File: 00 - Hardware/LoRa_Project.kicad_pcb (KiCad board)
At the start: 4 copper layers, 60 x 45 mm, 82 parts, among them IC1 MAX17048G+T10, IC2 E22-900M22S, J1 Conn_01x04_Pin, J2 USB_C_Receptacle_USB2.0_16P, J3 Conn_01x04_Pin, J4 Header_01x02_2.0mm JST PH, J5 SMA_ST_SMD, J6 Conn_01x04_Pin, U1 TPS2116DRLR, U2 MIC5219-3.3YM5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

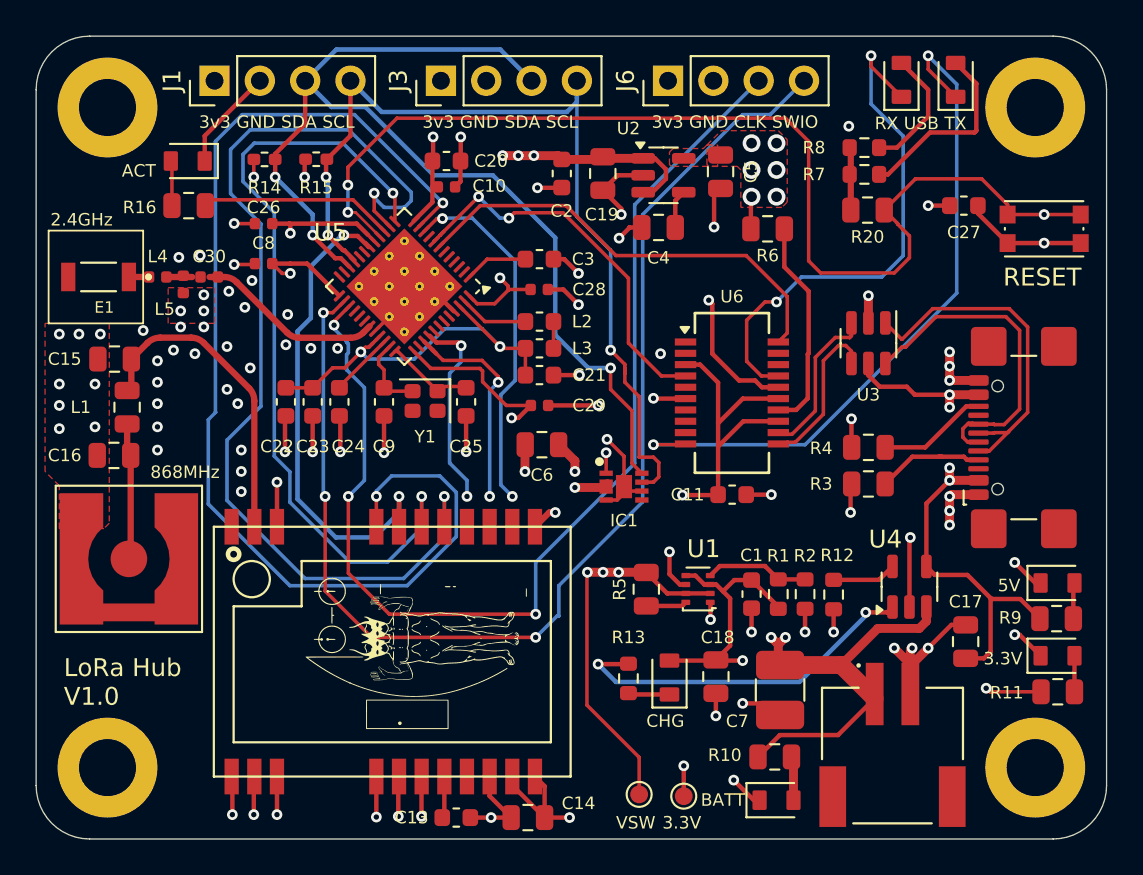
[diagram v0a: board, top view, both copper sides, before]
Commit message: updated FDTI cbus connections
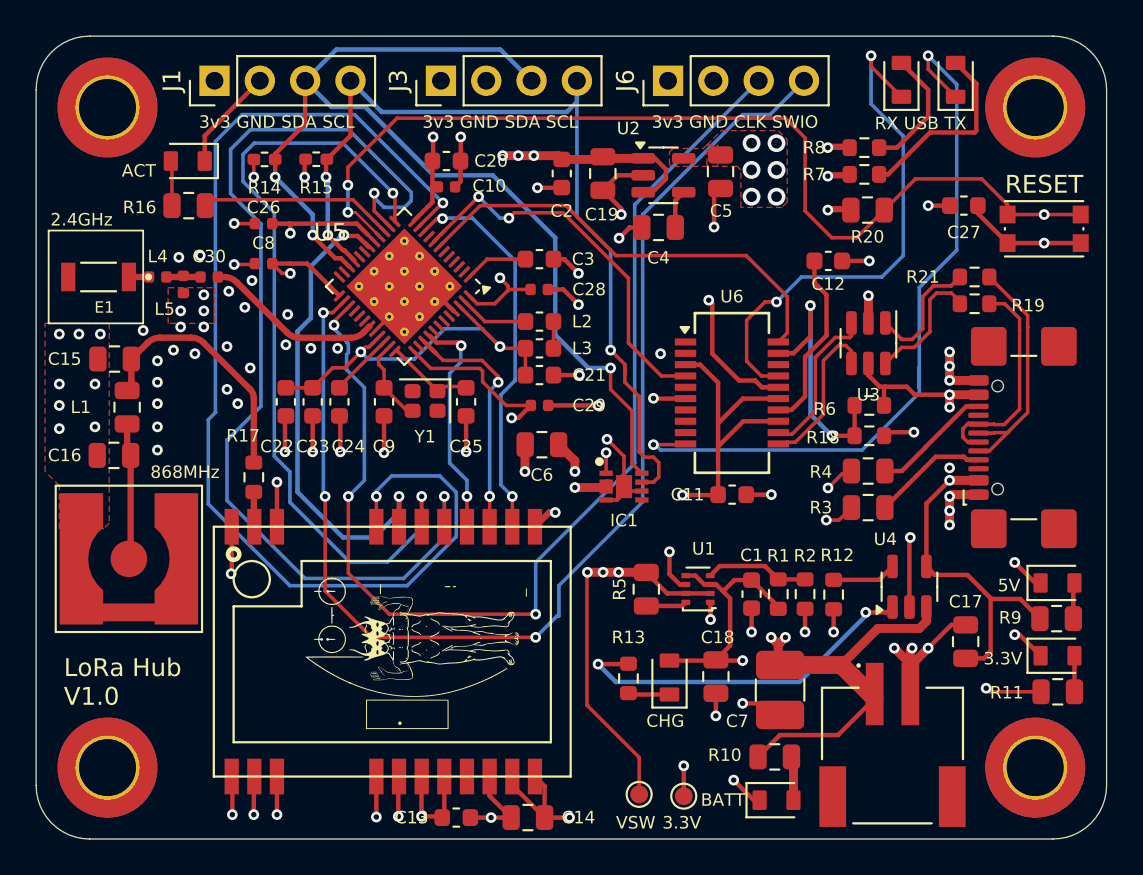
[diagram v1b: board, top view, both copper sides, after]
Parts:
- added C12: 100nF, Capacitor_SMD:C_0603_1608Metric, F.Cu at (234.4, 64.6)
- added R17: 0R_0603, Resistor_SMD:R_0603_1608Metric, F.Cu at (202.2, 76.7)
- added R18: 10K, Resistor_SMD:R_0603_1608Metric, F.Cu at (236.7, 74.4)
- added R19: 27, Resistor_SMD:R_0603_1608Metric, F.Cu at (242.6, 67.0)
- added R21: 27, Resistor_SMD:R_0603_1608Metric, F.Cu at (242.6, 65.5)
- H1, H2, H3, H4: value MountingHole_M3 -> MountingHole_Pad_M3; footprint Project_Footprints:MountingHole_3.2mm_M3_DIN965_Pad -> MountingHole:MountingHole_3.2mm_M3_DIN965_Pad_TopBottom
- R6: value 10K_0805 -> 4k7; footprint Project_Footprints:R_0805_2012Metric -> Resistor_SMD:R_0603_1608Metric
- moved R6 11.4 mm to (236.7, 72.7), turned to 180 degrees
- moved R3 1.33 mm to (236.6, 78.4)
- moved R4 1.33 mm to (236.6, 76.4)
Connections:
- C15 pad 1: Net-(IC2-ANT) -> Net-(C15-Pad1)
- L1 pad 1: Net-(IC2-ANT) -> Net-(C15-Pad1)
- R6 pad 1: +3V3 -> VBUS
- R6 pad 2: Net-(U6-~{RESET}) -> Net-(U6-CBUS3)
- U3 pad 1: /Power/USB_D- -> Net-(R21-Pad2)
- U3 pad 6: /Power/USB_D+ -> Net-(R19-Pad2)
- U5 pad 41: (no net) -> unconnected-(U5-P0.28-Pad41)
- U5 pad 42: (no net) -> unconnected-(U5-P0.29-Pad42)
- U5 pad 43: (no net) -> unconnected-(U5-P0.30-Pad43)
- U5 pad 44: (no net) -> unconnected-(U5-P0.31-Pad44)
- U5 pad 6: (no net) -> unconnected-(U5-P0.07-Pad6)
- U6 pad 19: unconnected-(U6-CBUS3-Pad19) -> Net-(U6-CBUS3)
- Y1 pad 2: Net-(U5-XC1) -> (no net)
- Y1 pad 3: (no net) -> Net-(U5-XC1)
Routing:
- net Net-(IC2-ANT): track 17.9 -> 1.96 mm
- net Net-(U6-CBUS3): track 0.00 -> 14.7 mm, vias 0 -> 2
- net Net-(C15-Pad1): track 0.00 -> 14.2 mm
- net Net-(R19-Pad2): track 0.00 -> 7.19 mm
- net Net-(R21-Pad2): track 0.00 -> 7.09 mm
- net Net-(U5-~{RESET}): track 61.5 -> 54.8 mm
- net GND: track 148.3 -> 154.7 mm
- net /Power/USB_D+: track 18.5 -> 12.3 mm
- net /Power/USB_D-: track 19.7 -> 13.9 mm
- net /Peripherals/TXLED: track 39.1 -> 42.6 mm
- net Net-(U6-~{RESET}): track 12.0 -> 10.2 mm
- net +3V3: track 68.3 -> 66.5 mm, vias 18 -> 20
- net /nRF52840 and LoRa/LORA_NRST: track 10.9 -> 12.6 mm
- net /nRF52840 and LoRa/LORA_IRQ: track 20.2 -> 21.9 mm
- net /nRF52840 and LoRa/LORA_BUSY: track 12.2 -> 13.9 mm
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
